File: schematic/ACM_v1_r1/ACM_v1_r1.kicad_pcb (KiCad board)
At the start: 4 copper layers, 25.5 x 39.9 mm, 34 parts, among them J1 DF40C-60DS-0.4V(51), J2 DF40C-60DS-0.4V(51), J3 Conn_02x04_Odd_Even, J4 Conn_01x02, J5 DF40C-60DS-0.4V(51), J6 DF40C-60DS-0.4V(51)

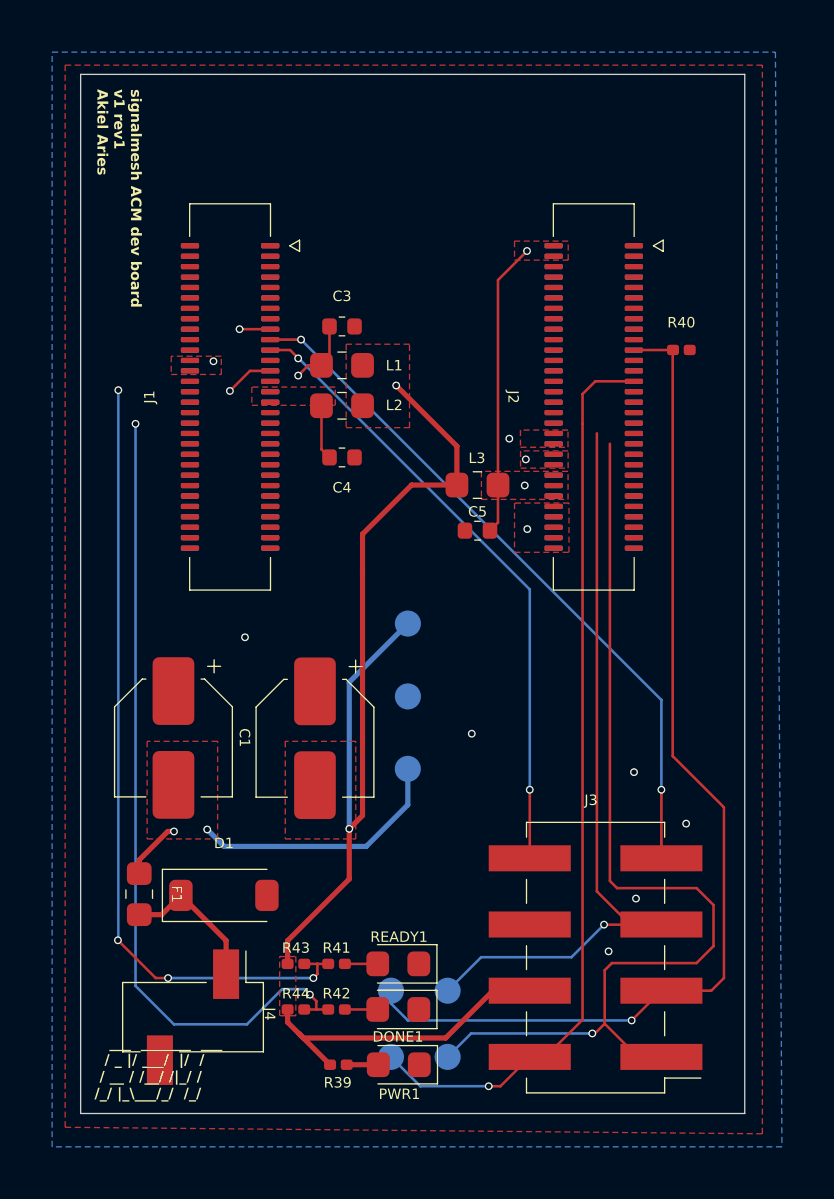
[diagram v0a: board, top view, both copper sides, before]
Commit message: figuring out FFC traces next
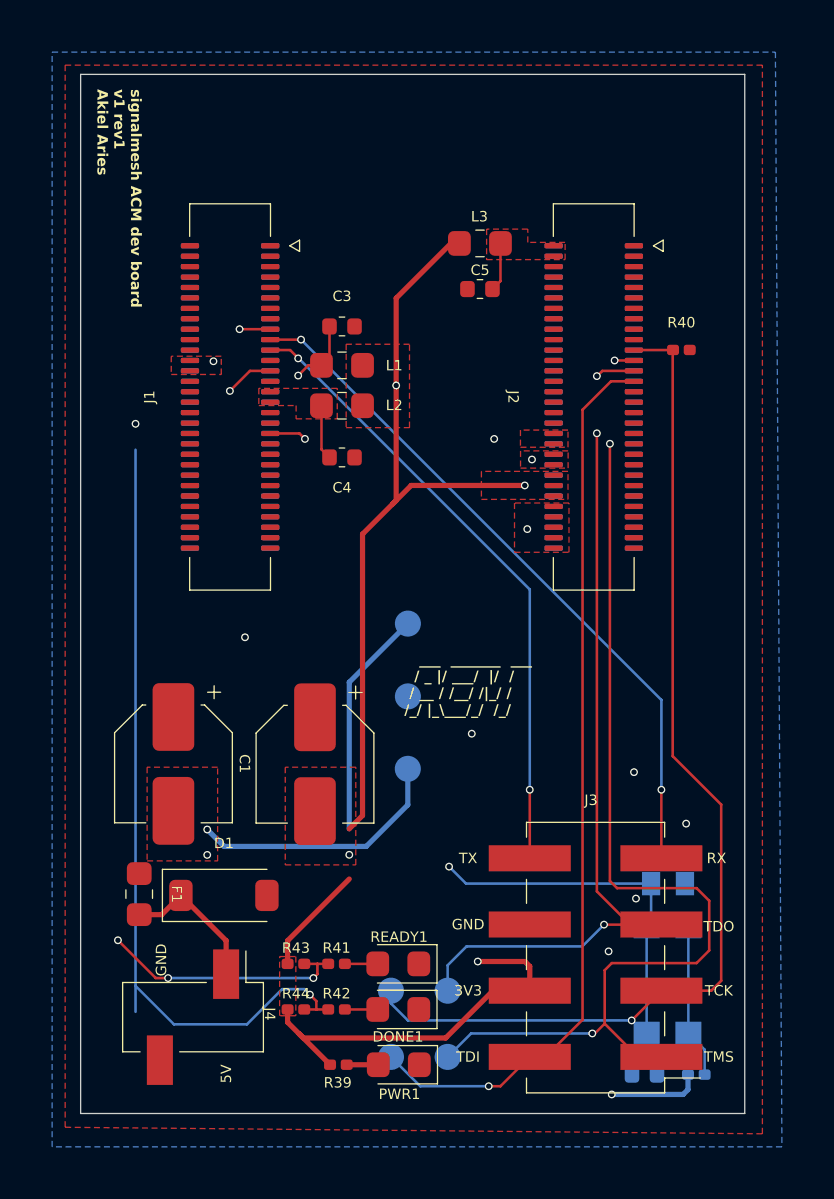
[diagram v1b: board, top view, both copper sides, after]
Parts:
- added C7: 100nF, Capacitor_SMD:C_0402_1005Metric, B.Cu at (151.7, 127.5)
- added L5: LXES15AAA1-153, my_footprints:INDC1005X45, B.Cu at (152.6, 120.2)
- added R45: 100R, Resistor_SMD:R_0201_0603Metric, B.Cu at (153.7, 127.5)
- added SW1: RST, Button_Switch_SMD:SW_Push_1P1T_NO_CK_KMR2, B.Cu at (152.6, 123.8)
- R39, R41, R42: value 49.9k -> 4.7k
- moved REF** 33.0 mm to (142.8, 92.7)
- moved C5 9.27 mm to (145.4, 97.3)
- moved L3 9.27 mm to (145.4, 95.6)
- moved G*** 4.14 mm to (141.5, 115.0), turned to -90 degrees
- moved C1 1.00 mm to (133.7, 115.6)
- moved C2 1.00 mm to (139.1, 115.6)
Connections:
- J5 pad 1: unconnected-(J5-Pin_1-Pad1) -> GND
- J5 pad 10: unconnected-(J5-Pin_10-Pad10) -> /FMC/K5_IOT63B
- J5 pad 11: unconnected-(J5-Pin_11-Pad11) -> /FMC/F7_IOT58A_40P
- J5 pad 12: unconnected-(J5-Pin_12-Pad12) -> /FMC/H8_IOT66A
- J5 pad 13: unconnected-(J5-Pin_13-Pad13) -> /FMC/F6_IOT58B_40P
- J5 pad 14: unconnected-(J5-Pin_14-Pad14) -> /FMC/H7_IOT66B
- J5 pad 15: unconnected-(J5-Pin_15-Pad15) -> GND
- J5 pad 16: unconnected-(J5-Pin_16-Pad16) -> /FMC/G7_IOT68A
- J5 pad 17: unconnected-(J5-Pin_17-Pad17) -> /FMC/E8_READY
- J5 pad 18: unconnected-(J5-Pin_18-Pad18) -> /FMC/G8_IOT68B
- J5 pad 19: unconnected-(J5-Pin_19-Pad19) -> /FMC/B3_IOB56A_FPGA_UART_RX
- J5 pad 2: unconnected-(J5-Pin_2-Pad2) -> GND
- J5 pad 20: unconnected-(J5-Pin_20-Pad20) -> /FMC/F5_IOT72A
- J5 pad 21: unconnected-(J5-Pin_21-Pad21) -> /FMC/C3_IOB56B_FPGA_UART_TX
- J5 pad 22: unconnected-(J5-Pin_22-Pad22) -> /FMC/G5_IOT72B
- J5 pad 23: unconnected-(J5-Pin_23-Pad23) -> /FMC/E3_IOB60A_40P
- J5 pad 24: unconnected-(J5-Pin_24-Pad24) -> /FMC/VCCIO0/1
- J5 pad 25: unconnected-(J5-Pin_25-Pad25) -> /FMC/D7_DONE
- J5 pad 26: unconnected-(J5-Pin_26-Pad26) -> /FMC/VCCIO0/1
- J5 pad 27: unconnected-(J5-Pin_27-Pad27) -> GND
- J5 pad 28: unconnected-(J5-Pin_28-Pad28) -> GND
- J5 pad 29: unconnected-(J5-Pin_29-Pad29) -> /FMC/VCCIO6/7
- J5 pad 3: unconnected-(J5-Pin_3-Pad3) -> /FMC/L9_IOT31A_40P
- J5 pad 30: unconnected-(J5-Pin_30-Pad30) -> /FMC/L6_IOT23A_USB_P
- J5 pad 31: unconnected-(J5-Pin_31-Pad31) -> /FMC/VCCIO6/7
- J5 pad 32: unconnected-(J5-Pin_32-Pad32) -> /FMC/K6_IOT23B_USB_N
- J5 pad 33: unconnected-(J5-Pin_33-Pad33) -> /FMC/J11_IOT1A_40P
- J5 pad 34: unconnected-(J5-Pin_34-Pad34) -> /FMC/K7_IOT21A_40P
- J5 pad 35: unconnected-(J5-Pin_35-Pad35) -> /FMC/J10_IOT1B_40P
- J5 pad 36: unconnected-(J5-Pin_36-Pad36) -> /FMC/J7_IOT21B_40P
- J5 pad 37: unconnected-(J5-Pin_37-Pad37) -> /FMC/H11_IOT3A_S1
- J5 pad 38: unconnected-(J5-Pin_38-Pad38) -> /FMC/L7_IOT19A_40P
- J5 pad 39: unconnected-(J5-Pin_39-Pad39) -> /FMC/H10_IOT3B_S2
- J5 pad 4: unconnected-(J5-Pin_4-Pad4) -> /FMC/H5_IOT61A
- J5 pad 40: unconnected-(J5-Pin_40-Pad40) -> /FMC/L8_IOT19B_40P
- J5 pad 41: unconnected-(J5-Pin_41-Pad41) -> /FMC/G11_IOT7A
- J5 pad 42: unconnected-(J5-Pin_42-Pad42) -> /FMC/L10_IOT15A_40P
- J5 pad 43: unconnected-(J5-Pin_43-Pad43) -> /FMC/G10_IOT7B
- J5 pad 44: unconnected-(J5-Pin_44-Pad44) -> /FMC/K10_IOT15B_40P
- J5 pad 45: unconnected-(J5-Pin_45-Pad45) -> GND
- J5 pad 46: unconnected-(J5-Pin_46-Pad46) -> /FMC/K11_IOT11A
- J5 pad 47: unconnected-(J5-Pin_47-Pad47) -> /FMC/D11_IOL9A
- J5 pad 48: unconnected-(J5-Pin_48-Pad48) -> /FMC/L11_IOT11B
- J5 pad 49: unconnected-(J5-Pin_49-Pad49) -> /FMC/D10_IOL9B
- J5 pad 5: unconnected-(J5-Pin_5-Pad5) -> /FMC/K9_IOT31B_40P
- J5 pad 50: unconnected-(J5-Pin_50-Pad50) -> GND
- J5 pad 51: unconnected-(J5-Pin_51-Pad51) -> /FMC/C11_IOL5A
- J5 pad 52: unconnected-(J5-Pin_52-Pad52) -> /FMC/E11_IOL3A
- J5 pad 53: unconnected-(J5-Pin_53-Pad53) -> /FMC/C10_IOL5B
- J5 pad 54: unconnected-(J5-Pin_54-Pad54) -> /FMC/E10_IOL3B
- J5 pad 55: unconnected-(J5-Pin_55-Pad55) -> /FMC/B11_IOL12A
- J5 pad 56: unconnected-(J5-Pin_56-Pad56) -> /FMC/A11_IOL14A
- J5 pad 57: unconnected-(J5-Pin_57-Pad57) -> /FMC/B10_IOL12B
- J5 pad 58: unconnected-(J5-Pin_58-Pad58) -> /FMC/A10_IOL14B
- J5 pad 59: unconnected-(J5-Pin_59-Pad59) -> GND
- J5 pad 6: unconnected-(J5-Pin_6-Pad6) -> /FMC/J5_IOT61B
- J5 pad 60: unconnected-(J5-Pin_60-Pad60) -> GND
- J5 pad 7: unconnected-(J5-Pin_7-Pad7) -> /FMC/J8_IOT56A_40P
- J5 pad 8: unconnected-(J5-Pin_8-Pad8) -> /FMC/L5_IOT63A
- J5 pad 9: unconnected-(J5-Pin_9-Pad9) -> /FMC/K8_IOT56B_40P
- J6 pad 1: unconnected-(J6-Pin_1-Pad1) -> GND
- J6 pad 10: unconnected-(J6-Pin_10-Pad10) -> /FMC/K1_IOR20A_40P
- J6 pad 11: unconnected-(J6-Pin_11-Pad11) -> /FMC/A1_IOB24A_40P
- J6 pad 12: unconnected-(J6-Pin_12-Pad12) -> /FMC/K2_IOR20B_40P
- J6 pad 13: unconnected-(J6-Pin_13-Pad13) -> /FMC/D8_RECONFIG
- J6 pad 14: unconnected-(J6-Pin_14-Pad14) -> /FMC/J4_IOR22A_40P
- J6 pad 15: unconnected-(J6-Pin_15-Pad15) -> /FMC/E1_IOB12B_40P
- J6 pad 16: unconnected-(J6-Pin_16-Pad16) -> /FMC/K4_IOR22B_40P
- J6 pad 17: unconnected-(J6-Pin_17-Pad17) -> /FMC/D1_IOB14B_40P
- J6 pad 18: unconnected-(J6-Pin_18-Pad18) -> /FMC/G2_IOR24A_40P
- J6 pad 19: unconnected-(J6-Pin_19-Pad19) -> GND
- J6 pad 2: unconnected-(J6-Pin_2-Pad2) -> /FMC/VCCIO2/3
- J6 pad 20: unconnected-(J6-Pin_20-Pad20) -> /FMC/G1_IOR24B_40P
- J6 pad 21: unconnected-(J6-Pin_21-Pad21) -> /FMC/C1_JTAG_TCK
- J6 pad 22: unconnected-(J6-Pin_22-Pad22) -> /FMC/L4_IOR31A_40P
- J6 pad 23: unconnected-(J6-Pin_23-Pad23) -> /FMC/B1_JTAG_TMS
- J6 pad 24: unconnected-(J6-Pin_24-Pad24) -> /FMC/L3_IOR31B_40P
- J6 pad 25: unconnected-(J6-Pin_25-Pad25) -> /FMC/A2_JTAG_TDO
- J6 pad 26: unconnected-(J6-Pin_26-Pad26) -> /FMC/J1_IOR33A_40P
- J6 pad 27: unconnected-(J6-Pin_27-Pad27) -> /FMC/A3_JTAG_TDI
- J6 pad 28: unconnected-(J6-Pin_28-Pad28) -> /FMC/J2_IOR33B_40P
- J6 pad 29: unconnected-(J6-Pin_29-Pad29) -> GND
- J6 pad 3: unconnected-(J6-Pin_3-Pad3) -> /FMC/B2_IOB4A_40P
- J6 pad 30: unconnected-(J6-Pin_30-Pad30) -> /FMC/G4_IOB89A_40P
- J6 pad 31: unconnected-(J6-Pin_31-Pad31) -> /FMC/M0_D3_P
- J6 pad 32: unconnected-(J6-Pin_32-Pad32) -> /FMC/H4_IOB89B_40P
- J6 pad 33: unconnected-(J6-Pin_33-Pad33) -> /FMC/M0_D3_N
- J6 pad 34: unconnected-(J6-Pin_34-Pad34) -> /FMC/H1_IOB91A_40P
- J6 pad 35: unconnected-(J6-Pin_35-Pad35) -> GND
- J6 pad 36: unconnected-(J6-Pin_36-Pad36) -> /FMC/H2_IOB91B_40P
- J6 pad 37: unconnected-(J6-Pin_37-Pad37) -> /FMC/M0_D2_P
- J6 pad 38: unconnected-(J6-Pin_38-Pad38) -> /FMC/VDD_1V8
- J6 pad 39: unconnected-(J6-Pin_39-Pad39) -> /FMC/M0_D2_N
- J6 pad 4: unconnected-(J6-Pin_4-Pad4) -> /FMC/VCCIO2/3
- J6 pad 40: unconnected-(J6-Pin_40-Pad40) -> /FMC/VDD_1V8
- J6 pad 41: unconnected-(J6-Pin_41-Pad41) -> GND
- J6 pad 42: unconnected-(J6-Pin_42-Pad42) -> /FMC/VDD_2V5
- J6 pad 43: unconnected-(J6-Pin_43-Pad43) -> /FMC/M0_CK_P
- J6 pad 44: unconnected-(J6-Pin_44-Pad44) -> /FMC/VDD_2V5
- J6 pad 45: unconnected-(J6-Pin_45-Pad45) -> /FMC/M0_CK_N
- J6 pad 46: unconnected-(J6-Pin_46-Pad46) -> /FMC/VDD_3V3
- J6 pad 47: unconnected-(J6-Pin_47-Pad47) -> GND
- J6 pad 48: unconnected-(J6-Pin_48-Pad48) -> /FMC/VDD_3V3
- J6 pad 49: unconnected-(J6-Pin_49-Pad49) -> /FMC/M0_D1_P
- J6 pad 5: unconnected-(J6-Pin_5-Pad5) -> /FMC/C2_IOB4B_40P
- J6 pad 50: unconnected-(J6-Pin_50-Pad50) -> /FMC/VDD_3V3
- J6 pad 51: unconnected-(J6-Pin_51-Pad51) -> /FMC/M0_D1_N
- J6 pad 52: unconnected-(J6-Pin_52-Pad52) -> +5V
- J6 pad 53: unconnected-(J6-Pin_53-Pad53) -> GND
- J6 pad 54: unconnected-(J6-Pin_54-Pad54) -> +5V
- J6 pad 55: unconnected-(J6-Pin_55-Pad55) -> /FMC/M0_D0_P
- J6 pad 56: unconnected-(J6-Pin_56-Pad56) -> +5V
- J6 pad 57: unconnected-(J6-Pin_57-Pad57) -> /FMC/M0_D0_N
- J6 pad 58: unconnected-(J6-Pin_58-Pad58) -> +5V
- J6 pad 59: unconnected-(J6-Pin_59-Pad59) -> GND
- J6 pad 6: unconnected-(J6-Pin_6-Pad6) -> /FMC/L2_IOR18A_40P
- J6 pad 60: unconnected-(J6-Pin_60-Pad60) -> +5V
- J6 pad 7: unconnected-(J6-Pin_7-Pad7) -> /FMC/F2_IOB26A_40P
- J6 pad 8: unconnected-(J6-Pin_8-Pad8) -> /FMC/L1_IOR18B_40P
- J6 pad 9: unconnected-(J6-Pin_9-Pad9) -> /FMC/F1_IOB26B_40P
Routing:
- net /H11_IOT3A_S1: track 0.00 -> 35.7 mm, vias 0 -> 2
- net +3V3: track 48.1 -> 69.1 mm, vias 3 -> 5
- net /VCCIO2/3: track 11.3 -> 1.88 mm, vias 1 -> 0
- net Net-(R45-Pad1): track 0.00 -> 5.94 mm
- net /A2_JTAG_TDO: track 29.8 -> 34.1 mm, vias 1 -> 3
- net /B1_JTAG_TMS: track 38.6 -> 42.4 mm, vias 1 -> 3
- net +5V: track 32.7 -> 30.4 mm
- net /E8_READY: vias 5 -> 4
- added copper zone on In1.Cu, net GND
- removed copper zone on In1.Cu, net +3V3
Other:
- board text added: "3V3"
- board text added: "5V"
- board text added: "GND"
- board text added: "RST"
- board text added: "RX"
- board text added: "TCK"
- board text added: "TDI"
- board text added: "TDO"
- board text added: "TMS"
- board text added: "TX"

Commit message: getting ACM and APM schematics put together. tool for FMC pin mapping verif
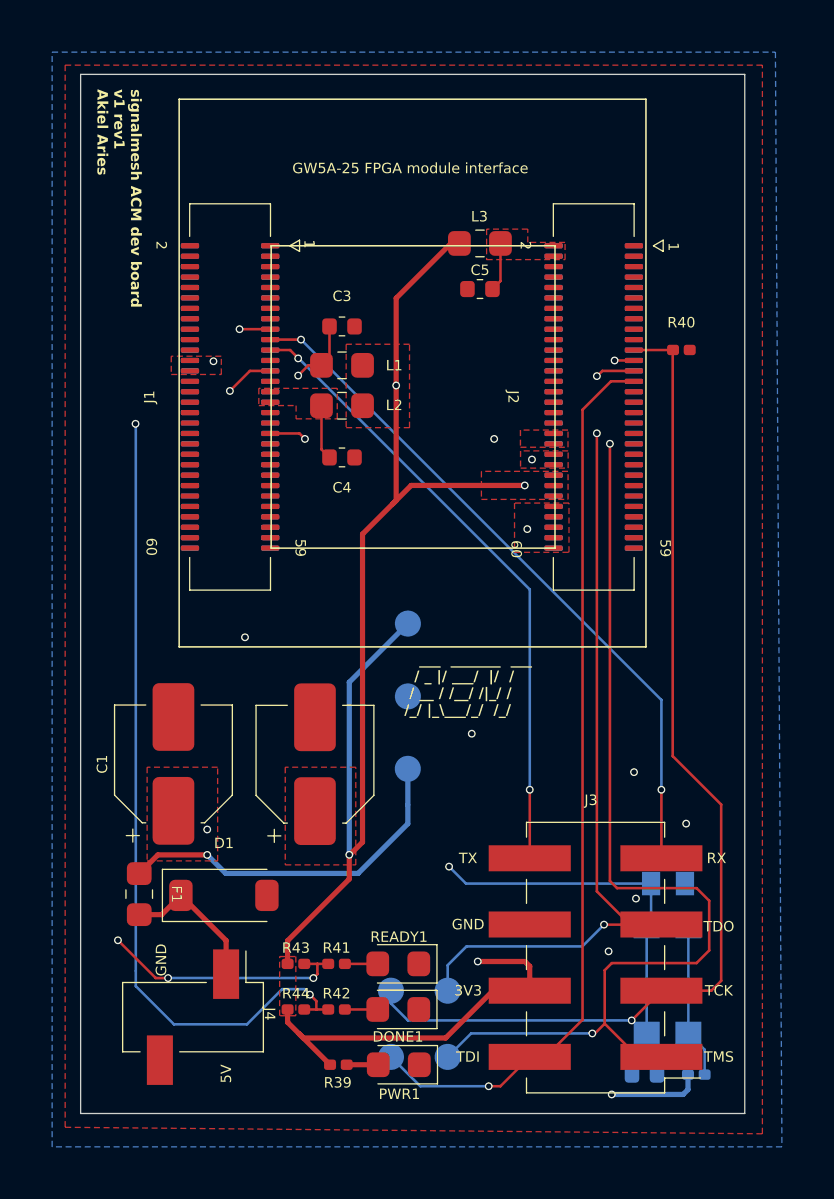
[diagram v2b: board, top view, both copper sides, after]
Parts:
- moved G*** 0.53 mm to (141.4, 114.5)
- turned C1 to 90 degrees
- turned C2 to 90 degrees
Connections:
- C1 pad 1: GND -> +5V
- C1 pad 2: +5V -> GND
- C2 pad 1: GND -> +3V3
- C2 pad 2: +3V3 -> GND
- J5 pad 10: /FMC/K5_IOT63B -> unconnected-(J5-Pin_10-Pad10)
- J5 pad 11: /FMC/F7_IOT58A_40P -> unconnected-(J5-Pin_11-Pad11)
- J5 pad 12: /FMC/H8_IOT66A -> unconnected-(J5-Pin_12-Pad12)
- J5 pad 13: /FMC/F6_IOT58B_40P -> unconnected-(J5-Pin_13-Pad13)
- J5 pad 14: /FMC/H7_IOT66B -> unconnected-(J5-Pin_14-Pad14)
- J5 pad 16: /FMC/G7_IOT68A -> /G7_IOT68A
- J5 pad 17: /FMC/E8_READY -> unconnected-(J5-Pin_17-Pad17)
- J5 pad 18: /FMC/G8_IOT68B -> /G8_IOT68B
- J5 pad 19: /FMC/B3_IOB56A_FPGA_UART_RX -> unconnected-(J5-Pin_19-Pad19)
- J5 pad 20: /FMC/F5_IOT72A -> /F5_IOT72A
- J5 pad 21: /FMC/C3_IOB56B_FPGA_UART_TX -> unconnected-(J5-Pin_21-Pad21)
- J5 pad 22: /FMC/G5_IOT72B -> /G5_IOT72B
- J5 pad 23: /FMC/E3_IOB60A_40P -> unconnected-(J5-Pin_23-Pad23)
- J5 pad 25: /FMC/D7_DONE -> unconnected-(J5-Pin_25-Pad25)
- J5 pad 3: /FMC/L9_IOT31A_40P -> unconnected-(J5-Pin_3-Pad3)
- J5 pad 30: /FMC/L6_IOT23A_USB_P -> /K6_IOT23B_USB_N
- J5 pad 32: /FMC/K6_IOT23B_USB_N -> /K7_IOT21A_40P
- J5 pad 33: /FMC/J11_IOT1A_40P -> unconnected-(J5-Pin_33-Pad33)
- J5 pad 34: /FMC/K7_IOT21A_40P -> unconnected-(J5-Pin_34-Pad34)
- J5 pad 35: /FMC/J10_IOT1B_40P -> /J10_IOT1B_40P
- J5 pad 36: /FMC/J7_IOT21B_40P -> unconnected-(J5-Pin_36-Pad36)
- J5 pad 37: /FMC/H11_IOT3A_S1 -> /H11_IOT3A_S1
- J5 pad 38: /FMC/L7_IOT19A_40P -> /L7_IOT19A_40P
- J5 pad 39: /FMC/H10_IOT3B_S2 -> /H10_IOT3B_S2
- J5 pad 4: /FMC/H5_IOT61A -> /H5_IOT61A
- J5 pad 40: /FMC/L8_IOT19B_40P -> /L8_IOT19B_40P
- J5 pad 41: /FMC/G11_IOT7A -> /G11_IOT7A
- J5 pad 42: /FMC/L10_IOT15A_40P -> /L10_IOT15A_40P
- J5 pad 43: /FMC/G10_IOT7B -> /G10_IOT7B
- J5 pad 44: /FMC/K10_IOT15B_40P -> /K10_IOT15B_40P
- J5 pad 46: /FMC/K11_IOT11A -> /K11_IOT11A
- J5 pad 47: /FMC/D11_IOL9A -> /D11_IOL9A
- J5 pad 48: /FMC/L11_IOT11B -> unconnected-(J5-Pin_48-Pad48)
- J5 pad 49: /FMC/D10_IOL9B -> /D10_IOL9B
- J5 pad 5: /FMC/K9_IOT31B_40P -> unconnected-(J5-Pin_5-Pad5)
- J5 pad 51: /FMC/C11_IOL5A -> /C11_IOL5A
- J5 pad 52: /FMC/E11_IOL3A -> unconnected-(J5-Pin_52-Pad52)
- J5 pad 53: /FMC/C10_IOL5B -> /C10_IOL5B
- J5 pad 54: /FMC/E10_IOL3B -> unconnected-(J5-Pin_54-Pad54)
- J5 pad 55: /FMC/B11_IOL12A -> /B11_IOL12A
- J5 pad 56: /FMC/A11_IOL14A -> unconnected-(J5-Pin_56-Pad56)
- J5 pad 57: /FMC/B10_IOL12B -> /B10_IOL12B
- J5 pad 58: /FMC/A10_IOL14B -> unconnected-(J5-Pin_58-Pad58)
- J5 pad 6: /FMC/J5_IOT61B -> unconnected-(J5-Pin_6-Pad6)
- J5 pad 7: /FMC/J8_IOT56A_40P -> unconnected-(J5-Pin_7-Pad7)
- J5 pad 8: /FMC/L5_IOT63A -> unconnected-(J5-Pin_8-Pad8)
- J5 pad 9: /FMC/K8_IOT56B_40P -> unconnected-(J5-Pin_9-Pad9)
- J6 pad 10: /FMC/K1_IOR20A_40P -> unconnected-(J6-Pin_10-Pad10)
- J6 pad 11: /FMC/A1_IOB24A_40P -> /A1_IOB24A_40P
- J6 pad 12: /FMC/K2_IOR20B_40P -> unconnected-(J6-Pin_12-Pad12)
- J6 pad 13: /FMC/D8_RECONFIG -> unconnected-(J6-Pin_13-Pad13)
- J6 pad 14: /FMC/J4_IOR22A_40P -> /J4_IOR22A_40P
- J6 pad 15: /FMC/E1_IOB12B_40P -> /E1_IOB12B_40P
- J6 pad 16: /FMC/K4_IOR22B_40P -> /K4_IOR22B_40P
- J6 pad 17: /FMC/D1_IOB14B_40P -> /D1_IOB14B_40P
- J6 pad 18: /FMC/G2_IOR24A_40P -> unconnected-(J6-Pin_18-Pad18)
- J6 pad 20: /FMC/G1_IOR24B_40P -> /G1_IOR24B_40P
- J6 pad 22: /FMC/L4_IOR31A_40P -> unconnected-(J6-Pin_22-Pad22)
- J6 pad 24: /FMC/L3_IOR31B_40P -> /L3_IOR31B_40P
- J6 pad 26: /FMC/J1_IOR33A_40P -> /J1_IOR33A_40P
- J6 pad 28: /FMC/J2_IOR33B_40P -> /J2_IOR33B_40P
- J6 pad 3: /FMC/B2_IOB4A_40P -> /B2_IOB4A_40P
- J6 pad 30: /FMC/G4_IOB89A_40P -> unconnected-(J6-Pin_30-Pad30)
- J6 pad 31: /FMC/M0_D3_P -> unconnected-(J6-Pin_31-Pad31)
- J6 pad 32: /FMC/H4_IOB89B_40P -> unconnected-(J6-Pin_32-Pad32)
- J6 pad 33: /FMC/M0_D3_N -> unconnected-(J6-Pin_33-Pad33)
- J6 pad 34: /FMC/H1_IOB91A_40P -> /H1_IOB91A_40P
- J6 pad 36: /FMC/H2_IOB91B_40P -> /H2_IOB91B_40P
- J6 pad 37: /FMC/M0_D2_P -> unconnected-(J6-Pin_37-Pad37)
- J6 pad 39: /FMC/M0_D2_N -> unconnected-(J6-Pin_39-Pad39)
- J6 pad 43: /FMC/M0_CK_P -> unconnected-(J6-Pin_43-Pad43)
- J6 pad 45: /FMC/M0_CK_N -> unconnected-(J6-Pin_45-Pad45)
- J6 pad 49: /FMC/M0_D1_P -> unconnected-(J6-Pin_49-Pad49)
- J6 pad 5: /FMC/C2_IOB4B_40P -> /C2_IOB4B_40P
- J6 pad 51: /FMC/M0_D1_N -> unconnected-(J6-Pin_51-Pad51)
- J6 pad 55: /FMC/M0_D0_P -> unconnected-(J6-Pin_55-Pad55)
- J6 pad 57: /FMC/M0_D0_N -> unconnected-(J6-Pin_57-Pad57)
- J6 pad 6: /FMC/L2_IOR18A_40P -> unconnected-(J6-Pin_6-Pad6)
- J6 pad 7: /FMC/F2_IOB26A_40P -> /F2_IOB26A_40P
- J6 pad 8: /FMC/L1_IOR18B_40P -> unconnected-(J6-Pin_8-Pad8)
- J6 pad 9: /FMC/F1_IOB26B_40P -> /F1_IOB26B_40P
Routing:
- net +5V: track 30.4 -> 34.2 mm
- net +3V3: track 69.1 -> 72.2 mm
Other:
- board text added: "1"
- board text added: "2"
- board text added: "59"
- board text added: "60"
- board text added: "GW5A-25 FPGA module interface"

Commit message: seems like everything is routed? off by 1 error for I2C FPGA pins fixed?
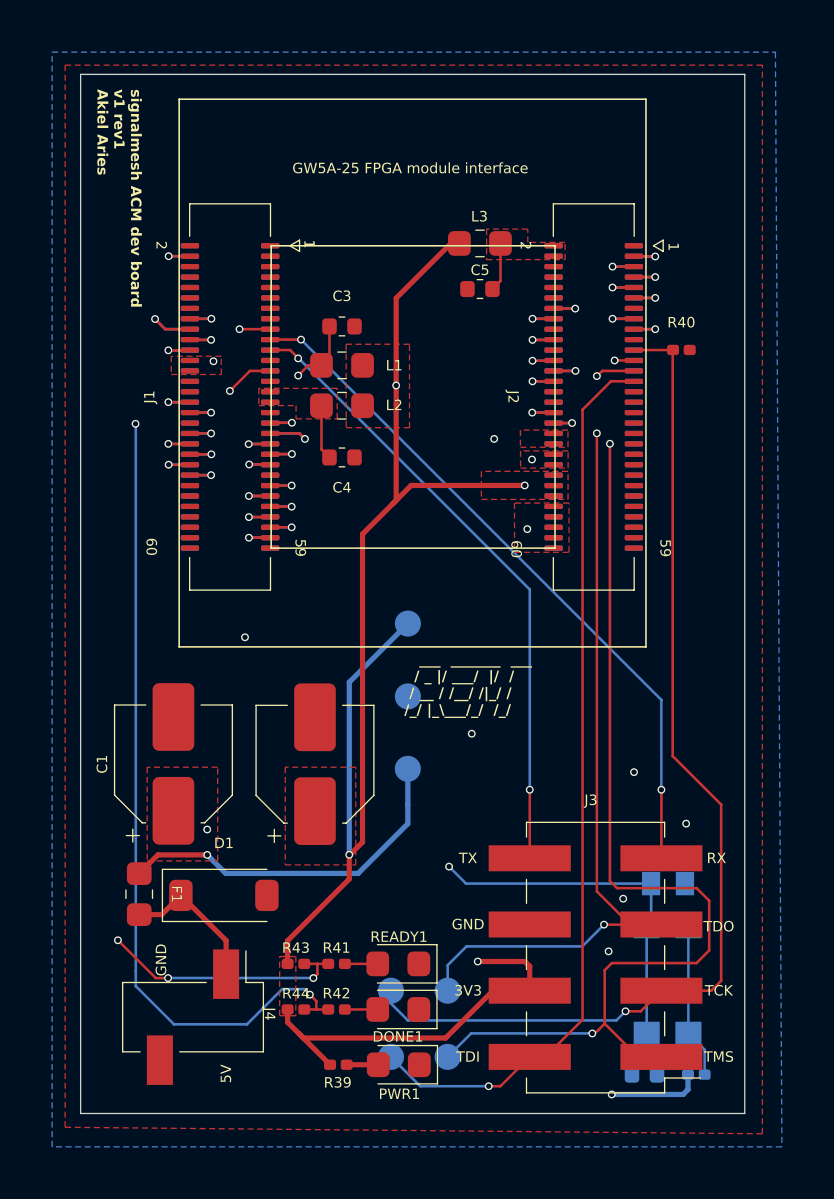
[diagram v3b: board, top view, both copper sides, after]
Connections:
- J5 pad 30: /K6_IOT23B_USB_N -> unconnected-(J5-Pin_30-Pad30)
- J5 pad 32: /K7_IOT21A_40P -> /K6_IOT23B_USB_N
- J5 pad 34: unconnected-(J5-Pin_34-Pad34) -> /K7_IOT21A_40P
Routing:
- net /G8_IOT68B: track 0.00 -> 3.00 mm, vias 0 -> 1
- net /H10_IOT3B_S2: track 0.00 -> 1.65 mm, vias 0 -> 1
- net /L10_IOT15A_40P: track 0.00 -> 1.64 mm, vias 0 -> 1
- net /J1_IOR33A_40P: track 0.00 -> 1.64 mm, vias 0 -> 1
- net /H1_IOB91A_40P: track 0.00 -> 1.64 mm, vias 0 -> 1
- net /G7_IOT68A: track 0.00 -> 1.64 mm, vias 0 -> 1
- net /L3_IOR31B_40P: track 0.00 -> 1.64 mm, vias 0 -> 1
- net /J2_IOR33B_40P: track 0.00 -> 1.64 mm, vias 0 -> 1
- net /G1_IOR24B_40P: track 0.00 -> 1.64 mm, vias 0 -> 1
- net /L8_IOT19B_40P: track 0.00 -> 1.64 mm, vias 0 -> 1
- net /L7_IOT19A_40P: track 0.00 -> 1.64 mm, vias 0 -> 1
- net /K7_IOT21A_40P: track 0.00 -> 1.64 mm, vias 0 -> 1
- net /K6_IOT23B_USB_N: track 0.00 -> 1.64 mm, vias 0 -> 1
- net /K4_IOR22B_40P: track 0.00 -> 1.64 mm, vias 0 -> 1
- net /K11_IOT11A: track 0.00 -> 1.64 mm, vias 0 -> 1
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
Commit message: schematic for the oscillator board
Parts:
- moved G*** 0.71 mm to (141.5, 115.2)
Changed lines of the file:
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@@
 	(footprint "graphics:obese_bulldog_15x16mm"
 		(layer "B.Cu")
-		(at 141.373938 114.502421 -90)
+		(at 141.473938 115.202421 -90)
 		(property "Reference" "G***"
 			(at 0 0 90)
